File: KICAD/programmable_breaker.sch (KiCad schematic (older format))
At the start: 2 parts

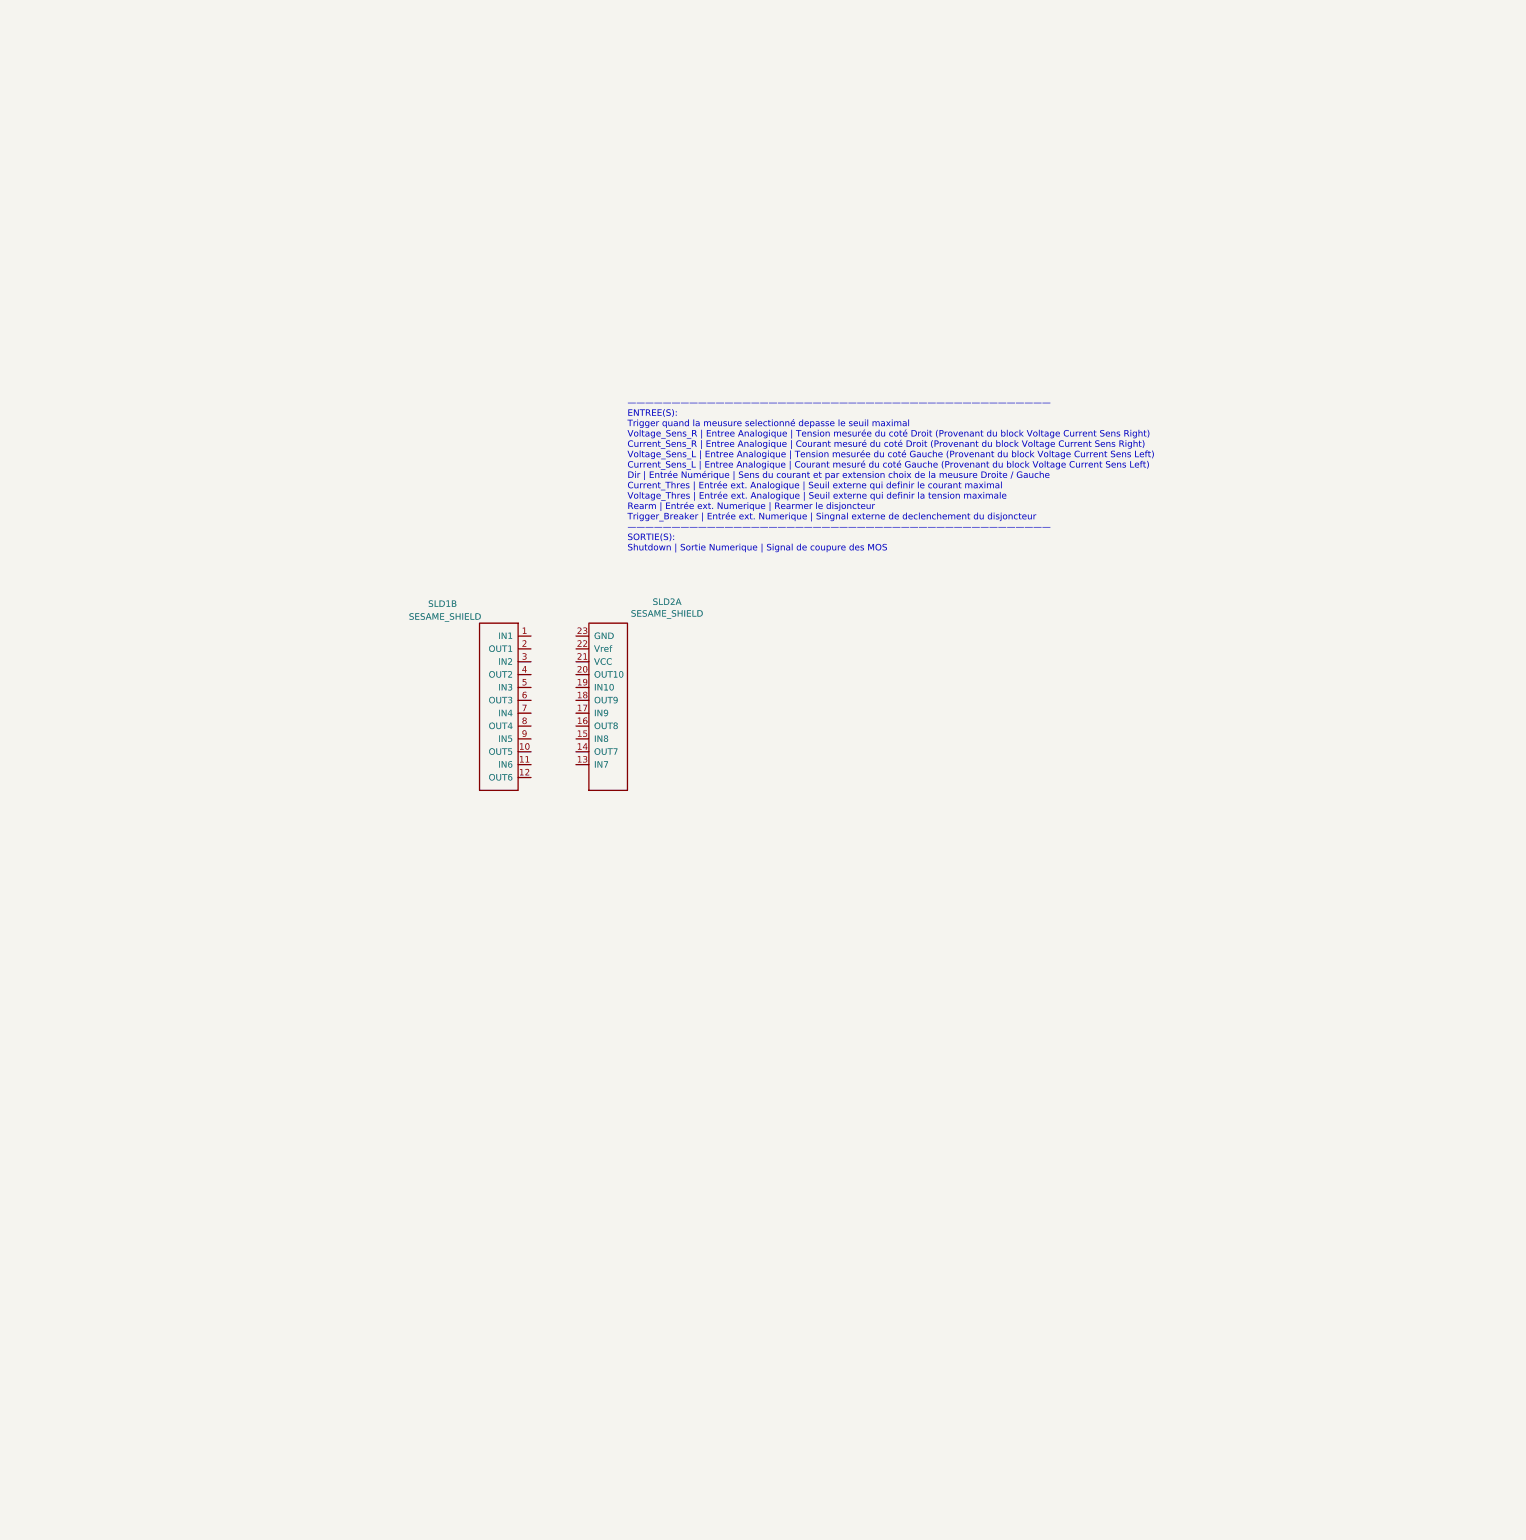
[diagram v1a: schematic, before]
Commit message: labels dans les blocks
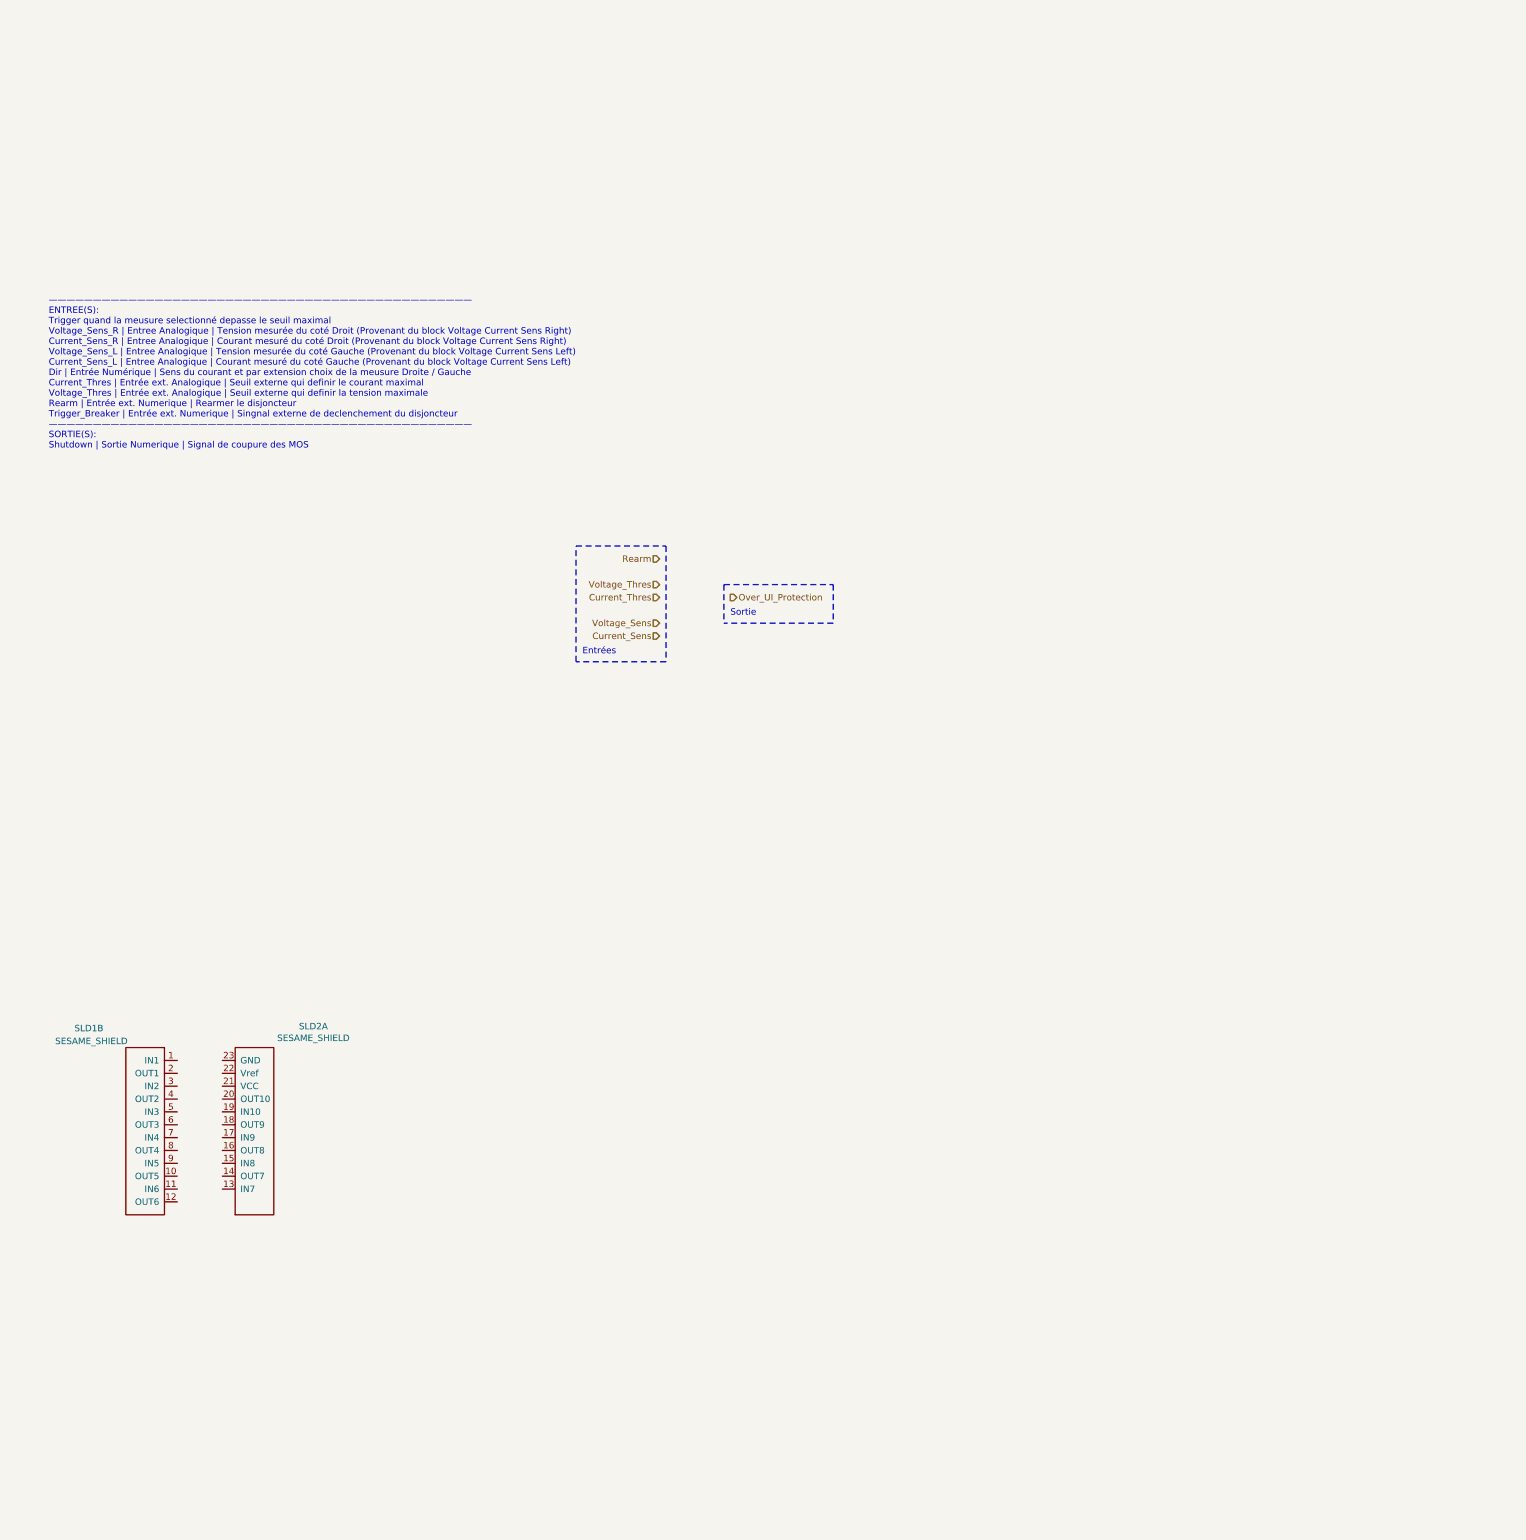
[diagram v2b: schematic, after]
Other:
- note added: "Entrées"
- note added: "Sortie"
- moved on the sheet: SLD1B, SLD2A
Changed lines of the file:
@@
 $Descr A4 11693 8268
 encoding utf-8
-Sheet 11 15
+Sheet 10 15
 Title "SESAME"
 Date ""
@@
 Comment4 ""
 $EndDescr
-Text Notes 5000 2500 0    50   ~ 0
+Text Notes 500  1700 0    50   ~ 0
 ————————————————————————————————————————————————\nENTREE(S):\nTrigger quand la meusure selectionné depasse le seuil maximal\nVoltage_Sens_R | Entree Analogique | Tension mesurée du coté Droit (Provenant du block Voltage Current Sens Right)\nCurrent_Sens_R | Entree Analogique | Courant mesuré du coté Droit (Provenant du block Voltage Current Sens Right)\nVoltage_Sens_L | Entree Analogique | Tension mesurée du coté Gauche (Provenant du block Voltage Current Sens Left)\nCurrent_Sens_L | Entree Analogique | Courant mesuré du coté Gauche (Provenant du block Voltage Current Sens Left)\nDir | Entrée Numérique | Sens du courant et par extension choix de la meusure Droite / Gauche\nCurrent_Thres | Entrée ext. Analogique | Seuil externe qui definir le courant maximal\nVoltage_Thres | Entrée ext. Analogique | Seuil externe qui definir la tension maximale\nRearm | Entrée ext. Numerique | Rearmer le disjoncteur\nTrigger_Breaker | Entrée ext. Numerique | Singnal externe de declenchement du disjoncteur\n————————————————————————————————————————————————\nSORTIE(S):\nShutdown | Sortie Numerique | Signal de coupure des MOS\n
 $Comp
 L Sesame:SESAME_SHIELD SLD1
 U 2 1 618C4894
-P 3800 3150
-F 0 "SLD1" H 3450 3400 50  0000 L CNN
-F 1 "SESAME_SHIELD" H 3300 3300 50  0000 L CNN
-F 2 "" H 3950 1900 50  0001 C CNN
-F 3 "" H 3950 1900 50  0001 C CNN
-	2    3800 3150
+P 1050 6450
+F 0 "SLD1" H 700 6700 50  0000 L CNN
+F 1 "SESAME_SHIELD" H 550 6600 50  0000 L CNN
+F 2 "" H 1200 5200 50  0001 C CNN
+F 3 "" H 1200 5200 50  0001 C CNN
+	2    1050 6450
 	1    0    0    -1
 $EndComp
@@
 L Sesame:SESAME_SHIELD SLD2
 U 1 1 618C53DC
-P 4250 3150
-F 0 "SLD2" H 5308 3415 50  0000 C CNN
-F 1 "SESAME_SHIELD" H 5308 3324 50  0000 C CNN
-F 2 "" H 4400 1900 50  0001 C CNN
-F 3 "" H 4400 1900 50  0001 C CNN
-	1    4250 3150
+P 1500 6450
+F 0 "SLD2" H 2558 6715 50  0000 C CNN
+F 1 "SESAME_SHIELD" H 2558 6624 50  0000 C CNN
+F 2 "" H 1650 5200 50  0001 C CNN
+F 3 "" H 1650 5200 50  0001 C CNN
+	1    1500 6450
 	1    0    0    -1
 $EndComp
+Text HLabel 5250 2550 0    50   Input ~ 0
+Rearm
+Text HLabel 5250 2750 0    50   Input ~ 0
+Voltage_Thres
+Text HLabel 5250 2850 0    50   Input ~ 0
+Current_Thres
+Text HLabel 5250 3050 0    50   Input ~ 0
+Voltage_Sens
+Text HLabel 5250 3150 0    50   Input ~ 0
+Current_Sens
+Text HLabel 5800 2850 2    50   Output ~ 0
+Over_UI_Protection
+Text Notes 5800 3000 0    50   ~ 0
+Sortie
+Text Notes 4650 3300 0    50   ~ 0
+Entrées
+Wire Notes Line
+	5750 2750 6600 2750
+Wire Notes Line
+	6600 2750 6600 3050
+Wire Notes Line
+	6600 3050 5750 3050
+Wire Notes Line
+	5750 2750 5750 3050
+Wire Notes Line
+	5300 2450 5300 3350
+Wire Notes Line
+	5300 3350 4600 3350
+Wire Notes Line
+	4600 3350 4600 2450
+Wire Notes Line
+	4600 2450 5300 2450
 $EndSCHEMATC

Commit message: merge program breaker nicolas
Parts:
- added C? (x3): C, symbol Device:C
- added C?: 10n, symbol Device:C
- added C?: 100n, symbol Device:C
- added JP? (x6): Jumper, symbol Device:Jumper
- added Q? (x5): BC847, Package_TO_SOT_SMD:SOT-23, symbol Transistor_BJT:BC847
- added R? (x7): R, symbol Device:R
- added R? (x3): 10k, symbol Device:R
- added R? (x5): 47k, symbol Device:R
- added RV? (x2): R_POT, symbol Device:R_POT
- added U? (x3): LM7332, symbol Amplifier_Operational:LM7332
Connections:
- net Current_Sens: now also R?.2
- net Current_Thres: now also JP?.1
- net Over_UI_Protection: now also C?.1, R?.1
- net Rearm: now also Q?.1 (B), R?.1
- net Voltage_Sens: now also R?.2
- net Voltage_Thres: now also JP?.1
- new net: C?.1, R?.1, U?.5 (+) (x2)
- new net: R?.1, U?.7 (x2)
- new net: Q?.1 (B), R?.2 (x2)
- new net: Q?.3 (C), R?.1, R?.2
- new net: Q?.1 (B), Q?.3 (C), Q?.3 (C), R?.2
- new net: C?.1, Q?.3 (C), R?.2, R?.2, R?.2
- new net: Q?.3 (C), R?.2, R?.2
- new net: Q?.1 (B), R?.1
- new net: JP?.2, JP?.2, JP?.2, U?.6 (-) (x2)
- new net: JP?.1, R?.1, R?.2 (x2)
- new net: JP?.1, RV?.2 (x2)
- new net GND: C?.2, C?.2, C?.2, C?.2, C?.2, Q?.2 (E), Q?.2 (E), Q?.2 (E), Q?.2 (E), Q?.2 (E), R?.2, R?.2, RV?.3, RV?.3, U?.8 (V+)
- new net VCC: C?.1, R?.1, R?.1, R?.1, R?.1, R?.1, RV?.1, RV?.1, U?.4 (V-)
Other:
- note added: "Alim. AOP"
- note added: "Amplification du signal de memoire"
- note added: "Bloc mémoire"
- note added: "Comparateur courant\n(Sur-courant)"
- note added: "comparateur tension\n(Sur-tension)"
- note removed: "Entrées"
- note removed: "Sortie"
- moved on the sheet: SLD1B, SLD2A
